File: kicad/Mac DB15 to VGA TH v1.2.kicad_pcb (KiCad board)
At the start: 2 copper layers, 44.5 x 39.6 mm, 12 parts, among them J1 Mac_DB15_Male_MountingHoles, J2 VGA_DB15_Female_HighDensity_M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

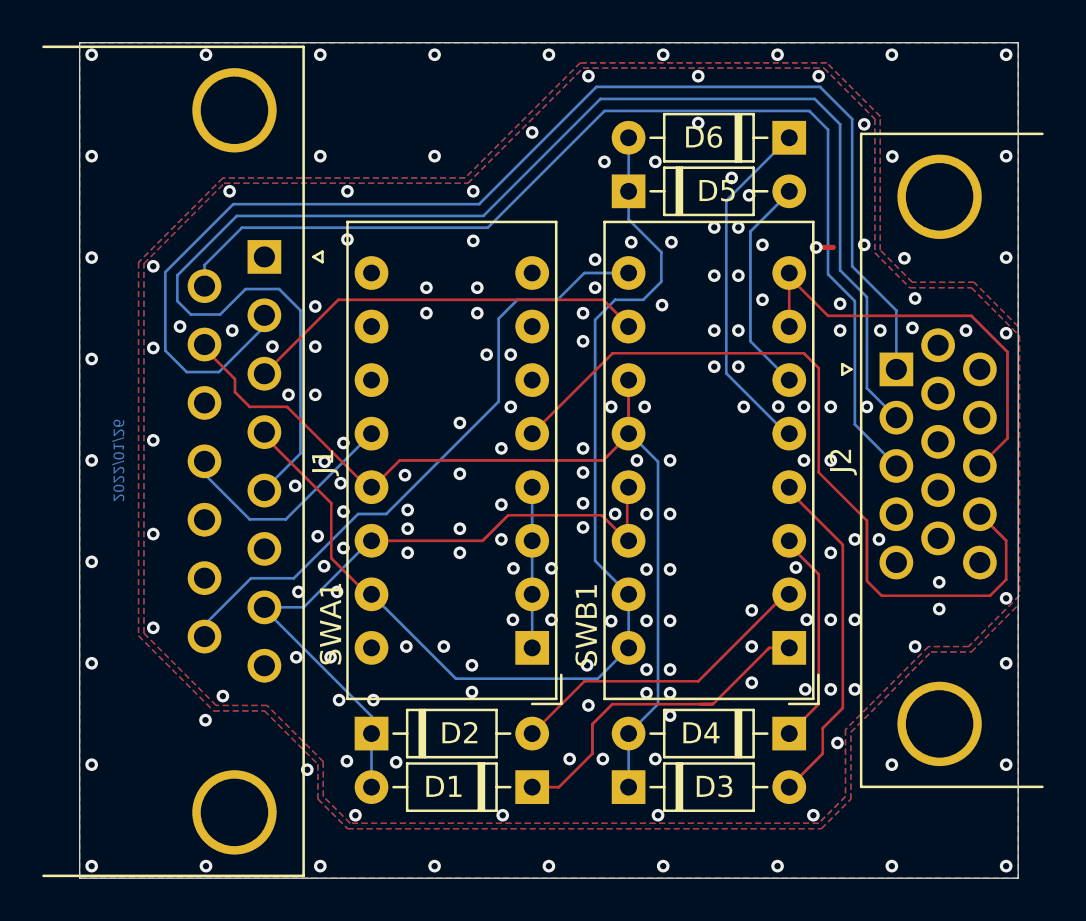
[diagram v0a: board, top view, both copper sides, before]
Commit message: Update all projects to Kicad 6.Remove unused snapeda footprint and symbol library references.
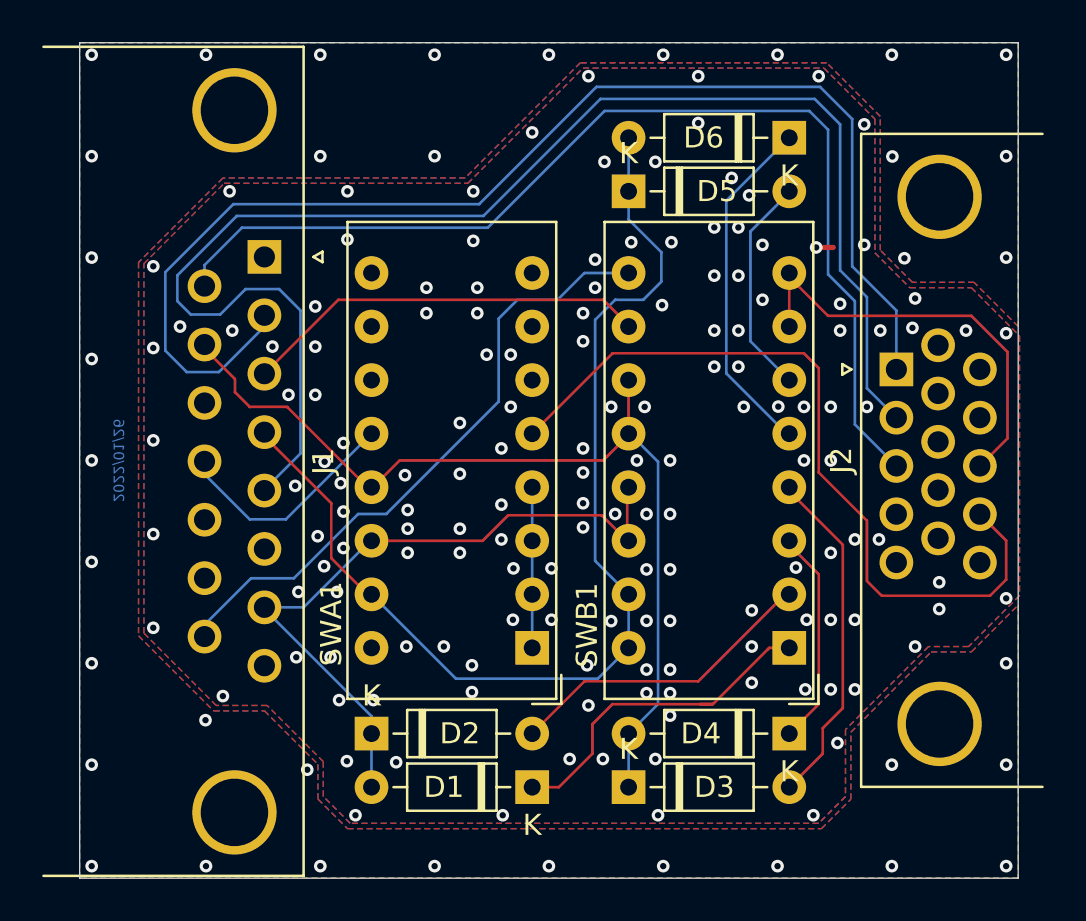
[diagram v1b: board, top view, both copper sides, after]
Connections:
- J1 pad 8: Net-(J1-Pad8) -> unconnected-(J1-Pad8)
- J2 pad 12: Net-(J2-Pad12) -> unconnected-(J2-Pad12)
- J2 pad 15: Net-(J2-Pad15) -> unconnected-(J2-Pad15)
- J2 pad 9: Net-(J2-Pad9) -> unconnected-(J2-Pad9)
- SWA1 pad 10: Net-(SWA1-Pad10) -> unconnected-(SWA1-Pad10)
- SWA1 pad 11: Net-(SWA1-Pad11) -> unconnected-(SWA1-Pad11)
- SWA1 pad 6: Net-(SWA1-Pad6) -> unconnected-(SWA1-Pad6)
- SWA1 pad 7: Net-(SWA1-Pad7) -> unconnected-(SWA1-Pad7)
- SWA1 pad 8: Net-(SWA1-Pad8) -> unconnected-(SWA1-Pad8)
- SWA1 pad 9: Net-(SWA1-Pad9) -> unconnected-(SWA1-Pad9)
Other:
- net class Default removed
